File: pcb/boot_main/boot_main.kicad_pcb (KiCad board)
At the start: 2 copper layers, 79 parts, among them J1 Conn_01x10_Pin, J2 Conn_01x02_Pin, P1 USB_C_Plug_USB2.0, Q1 NPN, Q2 NPN, Q3 NPN, SW1 SW_Push, SW2 SW_Push, U1 RP2040, U2 NCP1117-3.3_SOT223, U3 W25Q128JVS, U4 AT42QT1070-M, U5 W25Q32JVSS, Y1 Crystal_GND24

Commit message: Some initial layout
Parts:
- U3: value W25Q128JVS -> W25Q32JVZP; footprint Package_SO:SOIC-8_5.23x5.23mm_P1.27mm -> Package_SON:WSON-8-1EP_6x5mm_P1.27mm_EP3.4x4.3mm
- moved P1 82.6 mm to (204.4, 60.9), turned to 180 degrees
- moved R31 77.2 mm to (205.6, 66.8), turned to -90 degrees
- moved R30 74.5 mm to (202.7, 66.8), turned to -90 degrees
- moved C10 65.1 mm to (206.8, 85.4), turned to 90 degrees
- moved R1 64.8 mm to (203.7, 85.4), turned to -90 degrees
- moved C1 62.9 mm to (195.1, 64.1), turned to 180 degrees
- moved R2 62.3 mm to (204.7, 85.4), turned to -90 degrees
- moved U2 56.0 mm to (194.9, 69.6), turned to 180 degrees
- moved C7 53.0 mm to (205.8, 85.4), turned to 90 degrees
- moved C2 50.0 mm to (194.9, 75.6), turned to 0 degrees
- moved R33 42.5 mm to (195.1, 95.7), turned to -90 degrees
- moved C4 42.0 mm to (164.4, 28.4)
- moved R3 42.0 mm to (164.4, 30.9)
- moved R4 42.0 mm to (164.4, 33.4)
- moved U4 39.9 mm to (170.6, 91.3)
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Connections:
- U1 pad 3: unconnected-(U1-GPIO1-Pad3) -> /SCL
- U1 pad 4: unconnected-(U1-GPIO2-Pad4) -> /CAP_CHG
- U1 pad 5: unconnected-(U1-GPIO3-Pad5) -> /CAP_RES
- U1 pad 7: /SCL -> unconnected-(U1-GPIO5-Pad7)
- U1 pad 8: /CAP_RES -> unconnected-(U1-GPIO6-Pad8)
- U1 pad 9: /CAP_CHG -> unconnected-(U1-GPIO7-Pad9)
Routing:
- net +3V3: track 0.00 -> 37.1 mm
- net /SCL: track 0.00 -> 28.6 mm
- net /SDA: track 0.00 -> 28.3 mm
- net /CAP_CHG: track 0.00 -> 27.7 mm
- net /CAP_RES: track 0.00 -> 27.6 mm
- net /SPI_CS: track 0.00 -> 17.9 mm
- net /QSPI_SS: track 0.00 -> 17.6 mm
- net /SPI_RX: track 0.00 -> 16.6 mm, vias 0 -> 2
- net /QSPI_SD1: track 0.00 -> 16.4 mm
- net /QSPI_SD2: track 0.00 -> 15.5 mm
- net /Cap Sense/KEY6: track 0.00 -> 13.5 mm
- net VBUS: track 0.00 -> 13.0 mm
- net /Cap Sense/KEY5: track 0.00 -> 12.9 mm
- net /Cap Sense/KEY4: track 0.00 -> 12.3 mm
- net /SPI_TX: track 0.00 -> 11.7 mm
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
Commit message: MOre layout
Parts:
- added D13: LED, LED_SMD:LED_1206_3216Metric, F.Cu at (113.5, 30.5)
- added D14: LED, LED_SMD:LED_1206_3216Metric, F.Cu at (118.5, 35.5)
- added D15: LED, LED_SMD:LED_1206_3216Metric, F.Cu at (106.5, 47.5)
- added D16: LED, LED_SMD:LED_1206_3216Metric, F.Cu at (101.5, 42.5)
- added D17: LED, LED_SMD:LED_1206_3216Metric, F.Cu at (27.5, 42.5)
- added D18: LED, LED_SMD:LED_1206_3216Metric, F.Cu at (32.5, 47.5)
- added D19: LED, LED_SMD:LED_1206_3216Metric, F.Cu at (44.5, 35.5)
- added D20: LED, LED_SMD:LED_1206_3216Metric, F.Cu at (39.5, 30.5)
- added D21: LED, LED_SMD:LED_1206_3216Metric, F.Cu at (88.5, 30.5)
- added D22: LED, LED_SMD:LED_1206_3216Metric, F.Cu at (76.5, 42.5)
- added D23: LED, LED_SMD:LED_1206_3216Metric, F.Cu at (93.5, 35.5)
- added D24: LED, LED_SMD:LED_1206_3216Metric, F.Cu at (81.5, 47.5)
- added H1: MountingHole, MountingHole:MountingHole_3.2mm_M3, F.Cu at (21.5, 56.5)
- added H2: MountingHole, MountingHole:MountingHole_3.2mm_M3, F.Cu at (124.5, 56.5)
- added H3: MountingHole, MountingHole:MountingHole_3.2mm_M3, F.Cu at (124.5, 27.5)
- added H4: MountingHole, MountingHole:MountingHole_3.2mm_M3, F.Cu at (21.5, 27.5)
- added U6: ~, cap_pads:square_20x20mm_guide, F.Cu at (85.0, 39.0)
- added U7: ~, cap_pads:square_20x20mm_guide, F.Cu at (110.0, 39.0)
- added U8: ~, cap_pads:square_20x20mm_guide, F.Cu at (36.0, 39.0)
- C1, C10, C11, C12, C13, C14, C15, C16, C17, C18, C2, C5, C6, C7, C8, C9, R1, R10, R11, R12, R14, R2, R30, R31, R32, R33, R34, R5, R6, R7, R8, R9, U1, U2, U3, U4, U5, Y1: moved to B.Cu
- J1: footprint Connector_PinHeader_2.54mm:PinHeader_1x10_P2.54mm_Vertical -> Connector_FFC-FPC:Hirose_FH12-10S-0.5SH_1x10-1MP_P0.50mm_Horizontal; moved to B.Cu
- P1: footprint Connector_USB:USB_C_Receptacle_GCT_USB4105-xx-A_16P_TopMnt_Horizontal -> Connector_USB:USB_C_Receptacle_GCT_USB4115-03-C; moved to B.Cu
- moved R21 122.5 mm to (30.0, 35.5)
- moved D5 122.0 mm to (27.5, 35.5)
- moved R20 121.9 mm to (38.2, 38.2), turned to -90 degrees
- moved D8 121.8 mm to (32.5, 30.5), turned to 180 degrees
- moved R24 121.8 mm to (32.5, 33.0), turned to 180 degrees
- moved Q2 120.3 mm to (36.0, 38.0)
- moved C5 119.4 mm to (104.1, 29.2), turned to -90 degrees
- moved C6 119.4 mm to (108.7, 29.2), turned to -90 degrees
- moved Y1 119.2 mm to (106.4, 29.4), turned to 90 degrees
- moved R32 118.0 mm to (69.0, 27.6)
- moved R6 118.0 mm to (75.7, 27.6), turned to -90 degrees
- moved R14 116.9 mm to (108.7, 31.2), turned to -90 degrees
- moved R7 116.9 mm to (69.0, 28.6)
- moved J1 116.6 mm to (60.0, 34.0)
- moved R8 115.8 mm to (69.0, 29.6)
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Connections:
- D11 pad 1: Net-(D10-K) -> Net-(D11-K)
- D12 pad 1: Net-(D10-K) -> Net-(D12-K)
- D2 pad 1: Net-(D1-K) -> Net-(D14-A)
- D3 pad 1: Net-(D1-K) -> Net-(D15-A)
- D4 pad 1: Net-(D1-K) -> Net-(D16-A)
- D5 pad 1: Net-(D5-K) -> Net-(D17-A)
- D6 pad 1: Net-(D5-K) -> Net-(D18-A)
- D7 pad 1: Net-(D5-K) -> Net-(D19-A)
- D8 pad 1: Net-(D5-K) -> Net-(D20-A)
- D9 pad 1: Net-(D10-K) -> Net-(D21-A)
- J1 pad 3: /Cap Sense/GUARD -> /Cap Sense/KEY6
- J1 pad 4: /Cap Sense/KEY1 -> /Cap Sense/KEY5
- J1 pad 5: /Cap Sense/KEY2 -> /Cap Sense/KEY4
- J1 pad 7: /Cap Sense/KEY4 -> /Cap Sense/KEY2
- J1 pad 8: /Cap Sense/KEY5 -> /Cap Sense/KEY1
- J1 pad 9: /Cap Sense/KEY6 -> /Cap Sense/GUARD
- Q1 pad 1: Net-(D1-K) -> Net-(D13-K)
- Q2 pad 1: Net-(D5-K) -> Net-(D17-K)
- Q3 pad 1: Net-(D10-K) -> Net-(D21-K)
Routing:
- net Net-(D13-K): track 0.00 -> 32.2 mm
- net Net-(D17-K): track 0.00 -> 31.9 mm
- net Net-(D21-K): track 0.00 -> 31.0 mm
- net +3V3: track 37.1 -> 65.6 mm, vias 0 -> 8
- net VBUS: track 13.0 -> 27.9 mm
- net Net-(P1-VCONN): track 1.76 -> 9.60 mm
- net Net-(D14-A): track 0.00 -> 4.30 mm
- net Net-(D20-A): track 0.00 -> 4.20 mm
- net Net-(D19-A): track 0.00 -> 4.20 mm
- net Net-(D18-A): track 0.00 -> 4.20 mm
- net Net-(D17-A): track 0.00 -> 4.20 mm
- net Net-(D16-A): track 0.00 -> 4.20 mm
- net Net-(D11-K): track 0.00 -> 4.20 mm
- net Net-(D10-K): track 0.00 -> 4.20 mm
- net Net-(D21-A): track 0.00 -> 4.20 mm
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- added copper zone on In2.Cu, net +3V3
- added copper zone on B.Cu, net GND
- added copper zone on F.Cu, net GND
- added copper zone on In1.Cu, net GND
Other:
- board outline added: 110 x 36 mm
- copper layers 2 -> 4

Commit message: move cap sense ic to front panel
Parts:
- removed R10, R11, R12, R32, R7, R8, R9: 10k, Resistor_SMD:R_0402_1005Metric
- removed R5, R6: 4.7k, Resistor_SMD:R_0603_1608Metric
- removed U4: AT42QT1070-M, Package_DFN_QFN:VQFN-20-1EP_3x3mm_P0.45mm_EP1.55x1.55mm
- J1: value Conn_01x10_Pin -> Conn_01x06_Pin; footprint Connector_FFC-FPC:Hirose_FH12-10S-0.5SH_1x10-1MP_P0.50mm_Horizontal -> Connector_FFC-FPC:Hirose_FH12-6S-0.5SH_1x06-1MP_P0.50mm_Horizontal
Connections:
- J1 pad 2: GND -> /SDA
- J1 pad 3: /Cap Sense/KEY6 -> /CAP_RES
- J1 pad 4: /Cap Sense/KEY5 -> /CAP_CHG
- J1 pad 5: /Cap Sense/KEY4 -> /SCL
- J1 pad 6: /Cap Sense/KEY3 -> GND
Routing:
- net /CAP_CHG: track 27.7 -> 53.6 mm
- net /SCL: track 28.6 -> 54.2 mm
- net /CAP_RES: track 27.6 -> 52.9 mm
- net /SDA: track 28.3 -> 52.3 mm
- net /Cap Sense/GUARD: track 12.9 -> 0.00 mm
- net /Cap Sense/KEY1: track 12.1 -> 0.00 mm
- net /Cap Sense/KEY2: track 11.7 -> 0.00 mm
- net /Cap Sense/KEY3: track 11.4 -> 0.00 mm
- net /Cap Sense/KEY4: track 11.0 -> 0.00 mm
- net /Cap Sense/KEY5: track 10.6 -> 0.00 mm
- net /Cap Sense/KEY6: track 10.2 -> 0.00 mm
- net Net-(U4-OUT2/KEY6): track 5.80 -> 0.00 mm
- net Net-(U4-OUT1/KEY5): track 4.49 -> 0.00 mm
- net Net-(U4-KEY4): track 1.77 -> 0.00 mm
- net Net-(U4-KEY3): track 1.77 -> 0.00 mm
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
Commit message: More layout
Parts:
- removed C4: 0.1u, Capacitor_SMD:C_0603_1608Metric
- removed R3, R4: 10k, Resistor_SMD:R_0603_1608Metric
- C3, R13, R35, SW1, SW2: moved to B.Cu
- moved SW1 125.3 mm to (90.8, 54.8)
- moved R13 111.3 mm to (97.0, 54.8), turned to -90 degrees
- moved J2 107.9 mm to (112.0, 25.8), turned to 90 degrees
- moved R35 92.0 mm to (112.5, 33.3), turned to 90 degrees
- moved SW2 91.0 mm to (121.1, 34.8)
- moved C3 62.5 mm to (101.8, 53.2), turned to 180 degrees
- moved C2 37.8 mm to (121.5, 42.0), turned to 0 degrees
- moved U2 30.7 mm to (121.4, 47.8), turned to 90 degrees
- moved C11 26.3 mm to (140.2, 41.0)
- moved C1 23.9 mm to (116.7, 50.2), turned to 90 degrees
- moved R33 9.39 mm to (95.8, 28.9), turned to 0 degrees
- moved R34 5.91 mm to (92.6, 28.9), turned to 180 degrees
- moved C15 1.44 mm to (104.0, 43.8), turned to -90 degrees
- moved C18 1.34 mm to (96.8, 37.2)
- moved U5 0.68 mm to (95.8, 32.7)
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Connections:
- R35 pad 1: +3V3 -> /RUN
- R35 pad 2: Net-(R35-Pad2) -> +3V3
- SW2 pad 1: Net-(R35-Pad2) -> /RUN
- U1 pad 2: unconnected-(U1-GPIO0-Pad2) -> /B2_LIGHT
- U1 pad 26: +3V3 -> /RUN
- U1 pad 31: /B2_LIGHT -> unconnected-(U1-GPIO20-Pad31)
- U1 pad 34: /B3_LIGHT -> unconnected-(U1-GPIO22-Pad34)
- U1 pad 8: unconnected-(U1-GPIO6-Pad8) -> /B3_LIGHT
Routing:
- net /B2_LIGHT: track 1.53 -> 71.3 mm
- net /B3_LIGHT: track 1.28 -> 20.2 mm
- net /RUN: track 0.00 -> 16.8 mm
- net VBUS: track 27.9 -> 16.2 mm
- net +1V1: track 10.8 -> 22.4 mm
- net +3V3: track 67.2 -> 78.0 mm, vias 9 -> 20
- net Net-(R13-Pad2): track 0.00 -> 10.8 mm
- net /SWDIO: track 3.20 -> 12.2 mm
- net GND: track 2.62 -> 11.0 mm, vias 2 -> 17
- net /SWCLK: track 3.20 -> 11.3 mm
- net /QSPI_SS: track 17.6 -> 21.1 mm
- net Net-(U5-IO2): track 3.10 -> 6.49 mm
- net /B1_LIGHT: track 1.28 -> 3.16 mm
- net /SPI_CS: track 17.9 -> 16.5 mm
- net Net-(C6-Pad2): track 2.02 -> 3.03 mm
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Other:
- outline, holes or cut-outs redrawn

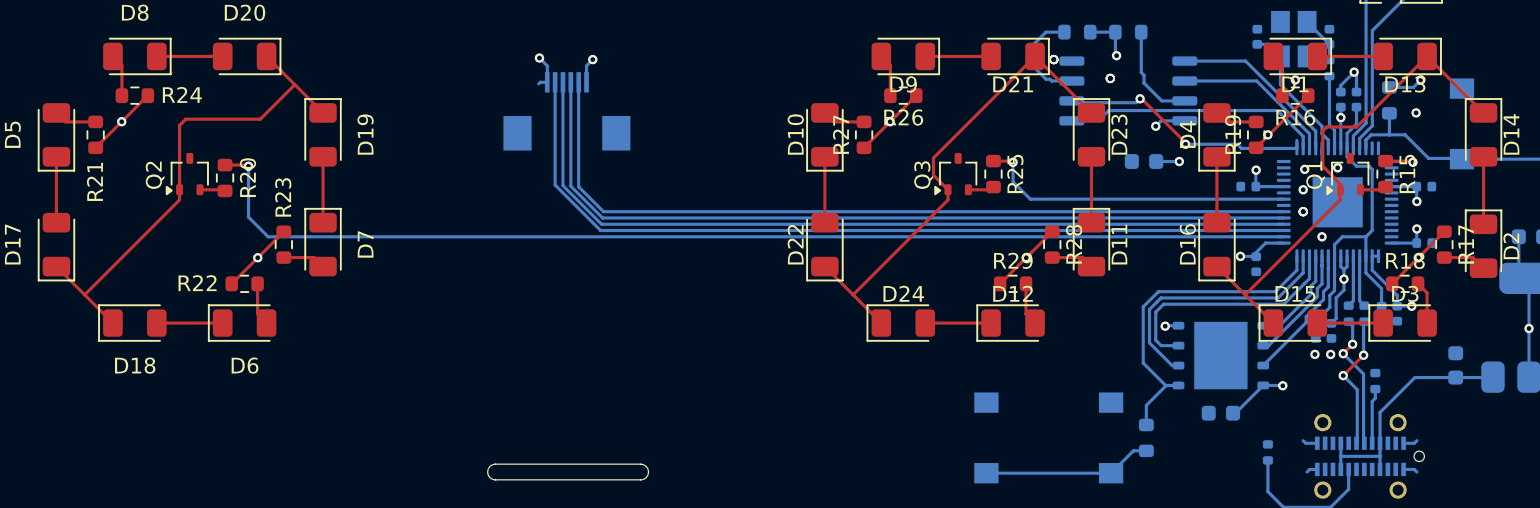
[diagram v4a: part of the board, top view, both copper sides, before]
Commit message: Change voltage rail on LEDs
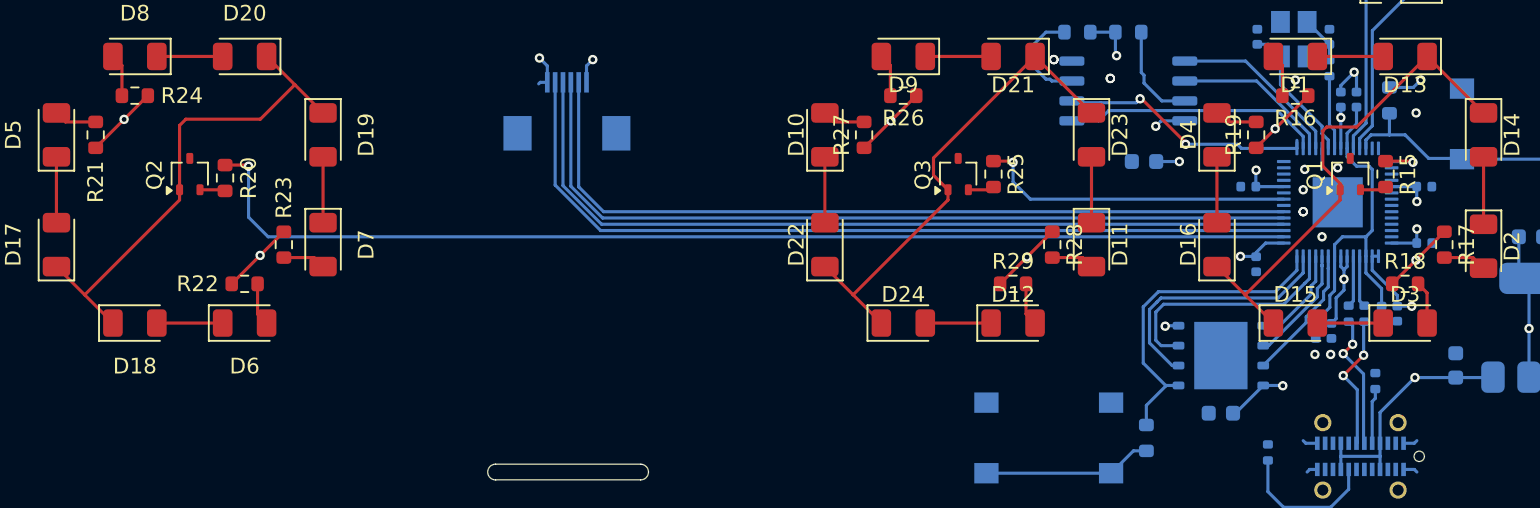
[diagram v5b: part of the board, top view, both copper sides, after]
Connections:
- R16 pad 1: +3V3 -> VBUS
- R17 pad 1: +3V3 -> VBUS
- R18 pad 1: +3V3 -> VBUS
- R19 pad 1: +3V3 -> VBUS
- R21 pad 1: +3V3 -> VBUS
- R22 pad 1: +3V3 -> VBUS
- R23 pad 1: +3V3 -> VBUS
- R24 pad 1: +3V3 -> VBUS
- R26 pad 1: +3V3 -> VBUS
- R27 pad 1: +3V3 -> VBUS
- R28 pad 1: +3V3 -> VBUS
- R29 pad 1: +3V3 -> VBUS
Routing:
- net VBUS: track 16.2 -> 188.7 mm, vias 0 -> 7
- net +3V3: track 78.0 -> 49.5 mm, vias 20 -> 14
